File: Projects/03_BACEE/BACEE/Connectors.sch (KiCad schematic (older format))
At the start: 4 parts

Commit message: Project 3: Arrange symbols
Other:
- moved on the sheet: J?
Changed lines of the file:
@@
 L Connector_Generic:Conn_01x09 J?
 U 1 1 61D286F6
-P 4350 3500
-F 0 "J?" H 4430 3542 50  0000 L CNN
-F 1 "Conn_01x09" H 4430 3451 50  0000 L CNN
-F 2 "" H 4350 3500 50  0001 C CNN
-F 3 "~" H 4350 3500 50  0001 C CNN
-	1    4350 3500
+P 5200 3500
+F 0 "J?" H 5280 3542 50  0000 L CNN
+F 1 "Conn_01x09" H 5280 3451 50  0000 L CNN
+F 2 "" H 5200 3500 50  0001 C CNN
+F 3 "~" H 5200 3500 50  0001 C CNN
+	1    5200 3500
 	1    0    0    -1
 $EndComp
@@
 L Connector_Generic:Conn_01x04 J?
 U 1 1 61D2A1E4
-P 5350 3500
-F 0 "J?" H 5430 3492 50  0000 L CNN
-F 1 "Conn_01x04" H 5430 3401 50  0000 L CNN
-F 2 "" H 5350 3500 50  0001 C CNN
-F 3 "~" H 5350 3500 50  0001 C CNN
-	1    5350 3500
+P 5200 2350
+F 0 "J?" H 5280 2342 50  0000 L CNN
+F 1 "Conn_01x04" H 5280 2251 50  0000 L CNN
+F 2 "" H 5200 2350 50  0001 C CNN
+F 3 "~" H 5200 2350 50  0001 C CNN
+	1    5200 2350
 	1    0    0    -1
 $EndComp
@@
 L Connector_Generic:Conn_02x03_Odd_Even J?
 U 1 1 61D2AF15
-P 4250 4550
-F 0 "J?" H 4300 4867 50  0000 C CNN
-F 1 "Conn_02x03_Odd_Even" H 4300 4776 50  0000 C CNN
-F 2 "" H 4250 4550 50  0001 C CNN
-F 3 "~" H 4250 4550 50  0001 C CNN
-	1    4250 4550
+P 6900 3600
+F 0 "J?" H 6950 3917 50  0000 C CNN
+F 1 "Conn_02x03_Odd_Even" H 6950 3826 50  0000 C CNN
+F 2 "" H 6900 3600 50  0001 C CNN
+F 3 "~" H 6900 3600 50  0001 C CNN
+	1    6900 3600
 	1    0    0    -1
 $EndComp
@@
 L Connector_Generic:Conn_01x04 J?
 U 1 1 61D2B784
-P 5350 4500
-F 0 "J?" H 5430 4492 50  0000 L CNN
-F 1 "Conn_01x04" H 5430 4401 50  0000 L CNN
-F 2 "" H 5350 4500 50  0001 C CNN
-F 3 "~" H 5350 4500 50  0001 C CNN
-	1    5350 4500
+P 6900 2350
+F 0 "J?" H 6980 2342 50  0000 L CNN
+F 1 "Conn_01x04" H 6980 2251 50  0000 L CNN
+F 2 "" H 6900 2350 50  0001 C CNN
+F 3 "~" H 6900 2350 50  0001 C CNN
+	1    6900 2350
 	1    0    0    -1
 $EndComp

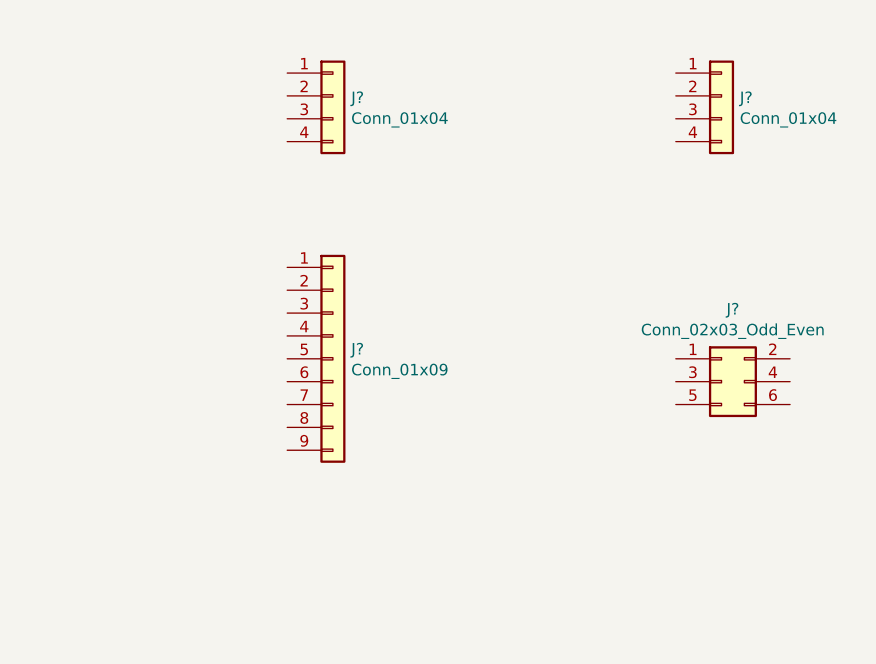
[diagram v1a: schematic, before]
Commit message: Project 3: Annotate schematic
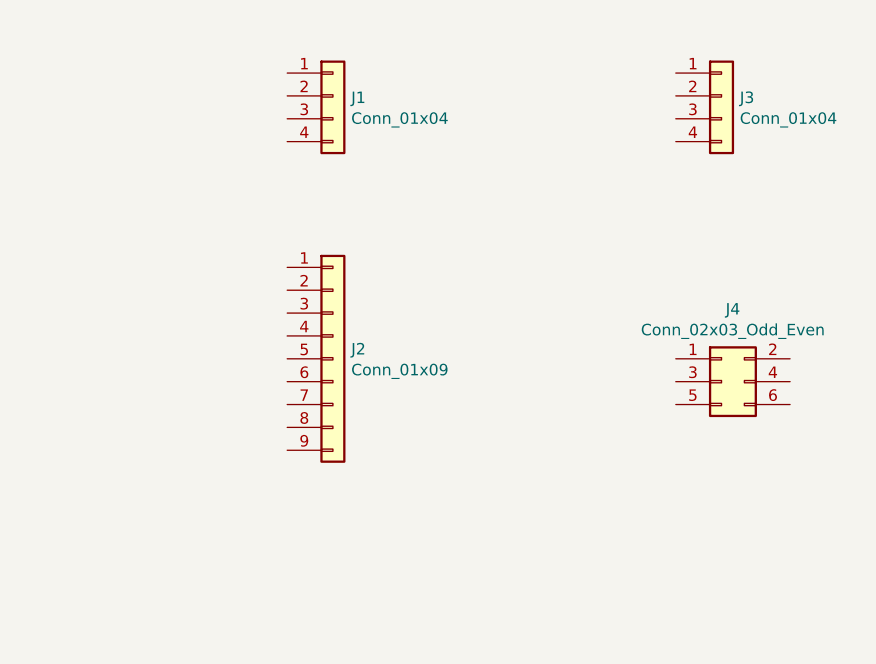
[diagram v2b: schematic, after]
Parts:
- gave numbers to parts that had none: 4
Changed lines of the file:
@@
 $EndDescr
 $Comp
-L Connector_Generic:Conn_01x09 J?
+L Connector_Generic:Conn_01x09 J2
 U 1 1 61D286F6
 P 5200 3500
-F 0 "J?" H 5280 3542 50  0000 L CNN
+F 0 "J2" H 5280 3542 50  0000 L CNN
 F 1 "Conn_01x09" H 5280 3451 50  0000 L CNN
 F 2 "" H 5200 3500 50  0001 C CNN
@@
 $EndComp
 $Comp
-L Connector_Generic:Conn_01x04 J?
+L Connector_Generic:Conn_01x04 J1
 U 1 1 61D2A1E4
 P 5200 2350
-F 0 "J?" H 5280 2342 50  0000 L CNN
+F 0 "J1" H 5280 2342 50  0000 L CNN
 F 1 "Conn_01x04" H 5280 2251 50  0000 L CNN
 F 2 "" H 5200 2350 50  0001 C CNN
@@
 $EndComp
 $Comp
-L Connector_Generic:Conn_02x03_Odd_Even J?
+L Connector_Generic:Conn_02x03_Odd_Even J4
 U 1 1 61D2AF15
 P 6900 3600
-F 0 "J?" H 6950 3917 50  0000 C CNN
+F 0 "J4" H 6950 3917 50  0000 C CNN
 F 1 "Conn_02x03_Odd_Even" H 6950 3826 50  0000 C CNN
 F 2 "" H 6900 3600 50  0001 C CNN
@@
 $EndComp
 $Comp
-L Connector_Generic:Conn_01x04 J?
+L Connector_Generic:Conn_01x04 J3
 U 1 1 61D2B784
 P 6900 2350
-F 0 "J?" H 6980 2342 50  0000 L CNN
+F 0 "J3" H 6980 2342 50  0000 L CNN
 F 1 "Conn_01x04" H 6980 2251 50  0000 L CNN
 F 2 "" H 6900 2350 50  0001 C CNN

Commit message: Project 3: Associate footprints
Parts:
- J1, J3: footprint (none) -> Connector_PinSocket_2.54mm:PinSocket_1x04_P2.54mm_Vertical
- J2: footprint (none) -> Connector_PinSocket_2.54mm:PinSocket_1x09_P2.54mm_Vertical
- J4: footprint (none) -> Connector_PinSocket_2.54mm:PinSocket_2x03_P2.54mm_Vertical
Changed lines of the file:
@@
 F 0 "J2" H 5280 3542 50  0000 L CNN
 F 1 "Conn_01x09" H 5280 3451 50  0000 L CNN
-F 2 "" H 5200 3500 50  0001 C CNN
+F 2 "Connector_PinSocket_2.54mm:PinSocket_1x09_P2.54mm_Vertical" H 5200 3500 50  0001 C CNN
 F 3 "~" H 5200 3500 50  0001 C CNN
 	1    5200 3500
@@
 F 0 "J1" H 5280 2342 50  0000 L CNN
 F 1 "Conn_01x04" H 5280 2251 50  0000 L CNN
-F 2 "" H 5200 2350 50  0001 C CNN
+F 2 "Connector_PinSocket_2.54mm:PinSocket_1x04_P2.54mm_Vertical" H 5200 2350 50  0001 C CNN
 F 3 "~" H 5200 2350 50  0001 C CNN
 	1    5200 2350
@@
 F 0 "J4" H 6950 3917 50  0000 C CNN
 F 1 "Conn_02x03_Odd_Even" H 6950 3826 50  0000 C CNN
-F 2 "" H 6900 3600 50  0001 C CNN
+F 2 "Connector_PinSocket_2.54mm:PinSocket_2x03_P2.54mm_Vertical" H 6900 3600 50  0001 C CNN
 F 3 "~" H 6900 3600 50  0001 C CNN
 	1    6900 3600
@@
 F 0 "J3" H 6980 2342 50  0000 L CNN
 F 1 "Conn_01x04" H 6980 2251 50  0000 L CNN
-F 2 "" H 6900 2350 50  0001 C CNN
+F 2 "Connector_PinSocket_2.54mm:PinSocket_1x04_P2.54mm_Vertical" H 6900 2350 50  0001 C CNN
 F 3 "~" H 6900 2350 50  0001 C CNN
 	1    6900 2350

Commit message: Project 3: Complete associations and add component values
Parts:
- J1: renamed from J2; value Conn_01x09 -> Digital Pins
- J2: renamed from J1; value Conn_01x04 -> Serial
- J4: renamed from J3; value Conn_01x04 -> I2C
- renumbered J4 to J3
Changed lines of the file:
@@
 $EndDescr
 $Comp
-L Connector_Generic:Conn_01x09 J2
+L Connector_Generic:Conn_01x04 J4
+U 1 1 61D2B784
+P 6900 2350
+F 0 "J4" H 6980 2342 50  0000 L CNN
+F 1 "I2C" H 6980 2251 50  0000 L CNN
+F 2 "Connector_PinSocket_2.54mm:PinSocket_1x04_P2.54mm_Vertical" H 6900 2350 50  0001 C CNN
+F 3 "~" H 6900 2350 50  0001 C CNN
+	1    6900 2350
+	1    0    0    -1
+$EndComp
+$Comp
+L Connector_Generic:Conn_01x09 J1
 U 1 1 61D286F6
 P 5200 3500
-F 0 "J2" H 5280 3542 50  0000 L CNN
-F 1 "Conn_01x09" H 5280 3451 50  0000 L CNN
+F 0 "J1" H 5280 3542 50  0000 L CNN
+F 1 "Digital Pins" H 5280 3451 50  0000 L CNN
 F 2 "Connector_PinSocket_2.54mm:PinSocket_1x09_P2.54mm_Vertical" H 5200 3500 50  0001 C CNN
 F 3 "~" H 5200 3500 50  0001 C CNN
@@
 $EndComp
 $Comp
-L Connector_Generic:Conn_01x04 J1
-U 1 1 61D2A1E4
-P 5200 2350
-F 0 "J1" H 5280 2342 50  0000 L CNN
-F 1 "Conn_01x04" H 5280 2251 50  0000 L CNN
-F 2 "Connector_PinSocket_2.54mm:PinSocket_1x04_P2.54mm_Vertical" H 5200 2350 50  0001 C CNN
-F 3 "~" H 5200 2350 50  0001 C CNN
-	1    5200 2350
-	1    0    0    -1
-$EndComp
-$Comp
-L Connector_Generic:Conn_02x03_Odd_Even J4
+L Connector_Generic:Conn_02x03_Odd_Even J3
 U 1 1 61D2AF15
 P 6900 3600
-F 0 "J4" H 6950 3917 50  0000 C CNN
+F 0 "J3" H 6950 3917 50  0000 C CNN
 F 1 "Conn_02x03_Odd_Even" H 6950 3826 50  0000 C CNN
 F 2 "Connector_PinSocket_2.54mm:PinSocket_2x03_P2.54mm_Vertical" H 6900 3600 50  0001 C CNN
@@
 $EndComp
 $Comp
-L Connector_Generic:Conn_01x04 J3
-U 1 1 61D2B784
-P 6900 2350
-F 0 "J3" H 6980 2342 50  0000 L CNN
-F 1 "Conn_01x04" H 6980 2251 50  0000 L CNN
-F 2 "Connector_PinSocket_2.54mm:PinSocket_1x04_P2.54mm_Vertical" H 6900 2350 50  0001 C CNN
-F 3 "~" H 6900 2350 50  0001 C CNN
-	1    6900 2350
+L Connector_Generic:Conn_01x04 J2
+U 1 1 61D2A1E4
+P 5200 2350
+F 0 "J2" H 5280 2342 50  0000 L CNN
+F 1 "Serial" H 5280 2251 50  0000 L CNN
+F 2 "Connector_PinSocket_2.54mm:PinSocket_1x04_P2.54mm_Vertical" H 5200 2350 50  0001 C CNN
+F 3 "~" H 5200 2350 50  0001 C CNN
+	1    5200 2350
 	1    0    0    -1
 $EndComp

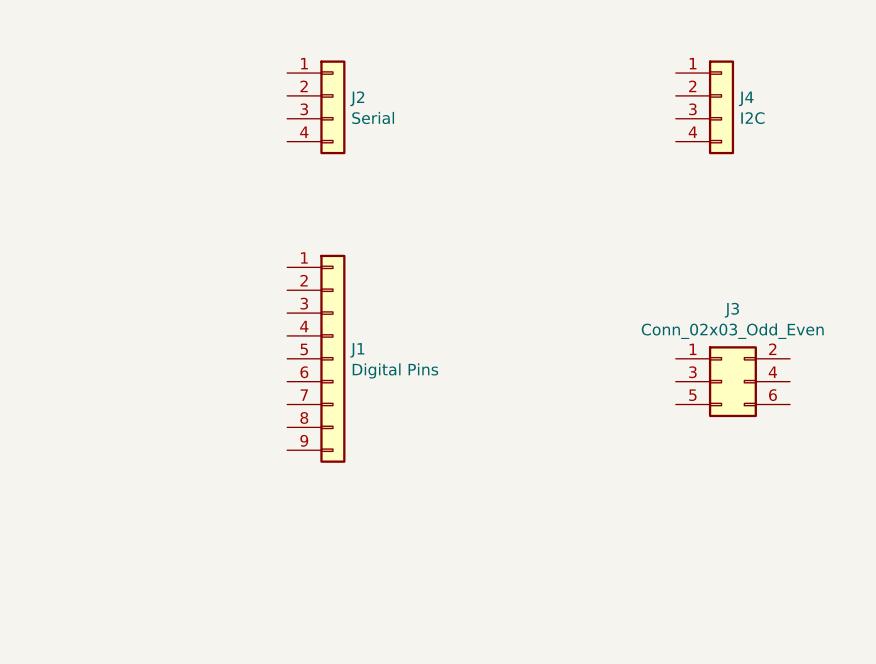
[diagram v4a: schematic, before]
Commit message: Project 3: Complete wiring of connectors hierarchical sheet
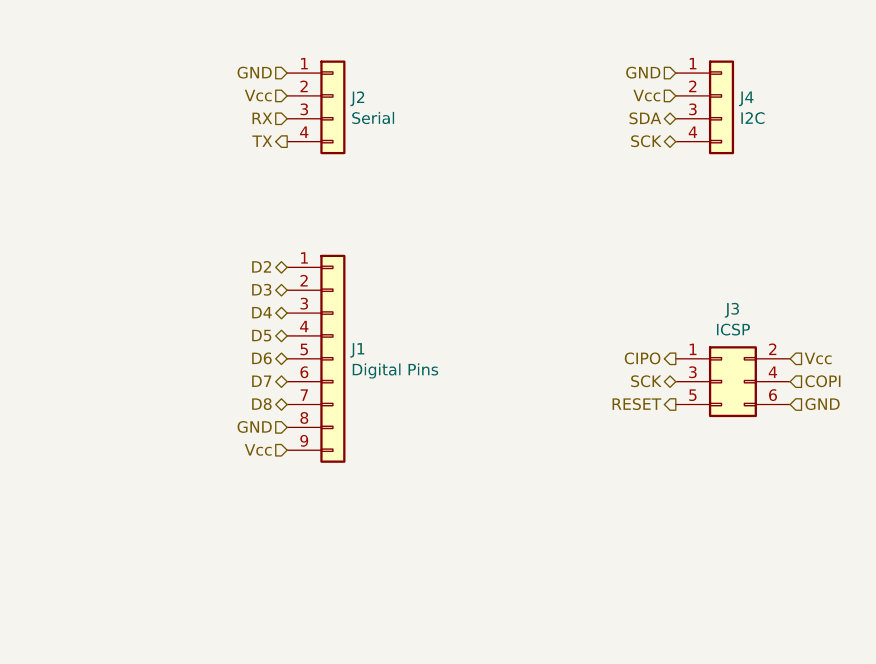
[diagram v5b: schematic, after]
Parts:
- J3: value Conn_02x03_Odd_Even -> ICSP
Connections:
- net D2: now reaches J1.1 (Pin_1)
- net D3: now reaches J1.2 (Pin_2)
- net D4: now reaches J1.3 (Pin_3)
- net D5: now reaches J1.4 (Pin_4)
- net D6: now reaches J1.5 (Pin_5)
- net D7: now reaches J1.6 (Pin_6)
- net D8: now reaches J1.7 (Pin_7)
- net GND: now reaches J1.8 (Pin_8)
- net GND: now also J2.1 (Pin_1), J3.6 (Pin_6), J4.1 (Pin_1)
- net Vcc: now reaches J1.9 (Pin_9)
- net Vcc: now also J2.2 (Pin_2), J3.2 (Pin_2), J4.2 (Pin_2)
- net RX: now reaches J2.3 (Pin_3)
- net TX: now reaches J2.4 (Pin_4)
- net CIPO: now reaches J3.1 (Pin_1)
- net SCK: now reaches J3.3 (Pin_3)
- net SCK: now also J4.4 (Pin_4)
- net COPI: now reaches J3.4 (Pin_4)
- net RESET: now reaches J3.5 (Pin_5)
- net SDA: now reaches J4.3 (Pin_3)
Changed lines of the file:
@@
 P 6900 3600
 F 0 "J3" H 6950 3917 50  0000 C CNN
-F 1 "Conn_02x03_Odd_Even" H 6950 3826 50  0000 C CNN
+F 1 "ICSP" H 6950 3826 50  0000 C CNN
 F 2 "Connector_PinSocket_2.54mm:PinSocket_2x03_P2.54mm_Vertical" H 6900 3600 50  0001 C CNN
 F 3 "~" H 6900 3600 50  0001 C CNN
@@
 	1    0    0    -1
 $EndComp
+Text HLabel 6700 3500 0    50   Output ~ 0
+CIPO
+Text HLabel 6700 3600 0    50   BiDi ~ 0
+SCK
+Text HLabel 6700 3700 0    50   Output ~ 0
+RESET
+Text HLabel 7200 3500 2    50   Input ~ 0
+Vcc
+Text HLabel 7200 3600 2    50   Input ~ 0
+COPI
+Text HLabel 7200 3700 2    50   Input ~ 0
+GND
+Text HLabel 5000 2250 0    50   Input ~ 0
+GND
+Text HLabel 5000 2350 0    50   Input ~ 0
+Vcc
+Text HLabel 5000 2450 0    50   Input ~ 0
+RX
+Text HLabel 5000 2550 0    50   Output ~ 0
+TX
+Text HLabel 6700 2250 0    50   Input ~ 0
+GND
+Text HLabel 6700 2350 0    50   Input ~ 0
+Vcc
+Text HLabel 6700 2450 0    50   BiDi ~ 0
+SDA
+Text HLabel 6700 2550 0    50   BiDi ~ 0
+SCK
+Text HLabel 5000 3100 0    50   BiDi ~ 0
+D2
+Text HLabel 5000 3200 0    50   BiDi ~ 0
+D3
+Text HLabel 5000 3300 0    50   BiDi ~ 0
+D4
+Text HLabel 5000 3400 0    50   BiDi ~ 0
+D5
+Text HLabel 5000 3500 0    50   BiDi ~ 0
+D6
+Text HLabel 5000 3600 0    50   BiDi ~ 0
+D7
+Text HLabel 5000 3700 0    50   BiDi ~ 0
+D8
+Text HLabel 5000 3900 0    50   Input ~ 0
+Vcc
+Text HLabel 5000 3800 0    50   Input ~ 0
+GND
 $EndSCHEMATC

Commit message: Project 3: Add functional block descriptions and generate netlist
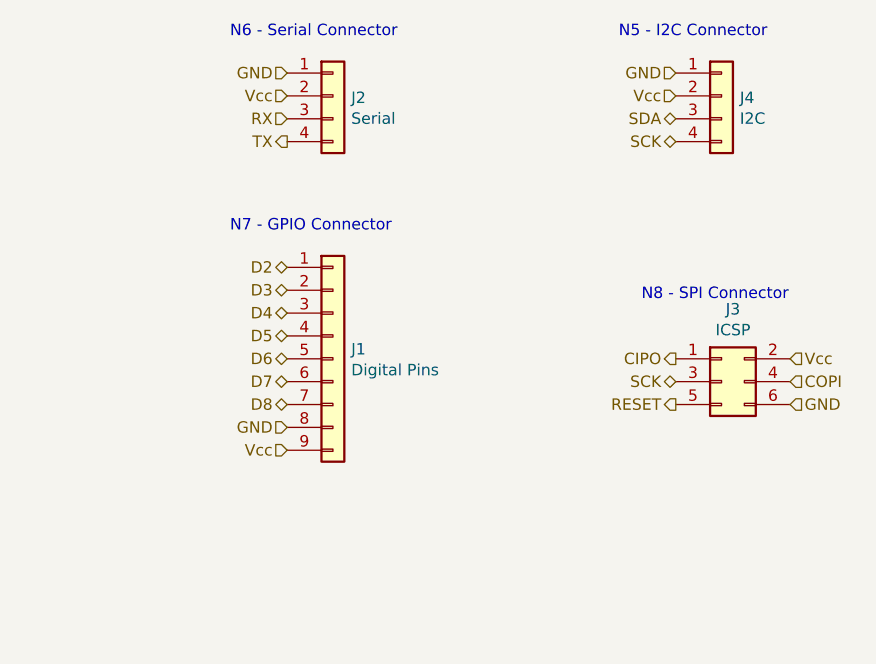
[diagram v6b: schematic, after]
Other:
- note added: "N5 - I2C Connector"
- note added: "N6 - Serial Connector"
- note added: "N7 - GPIO Connector"
- note added: "N8 - SPI Connector"
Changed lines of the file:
@@
 Text HLabel 5000 3800 0    50   Input ~ 0
 GND
+Text Notes 4750 2100 0    50   ~ 0
+N6 - Serial Connector
+Text Notes 6450 2100 0    50   ~ 0
+N5 - I2C Connector
+Text Notes 4750 2950 0    50   ~ 0
+N7 - GPIO Connector
+Text Notes 6550 3250 0    50   ~ 0
+N8 - SPI Connector
 $EndSCHEMATC
